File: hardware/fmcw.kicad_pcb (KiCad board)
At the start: 4 copper layers, 123.2 x 49.5 mm, 439 parts, among them CON1 SD_Card_DM3BT, CON2 BARREL_JACK, P1 SMA, P10 CONN_01X01, P11 CONN_01X01, P12 CONN_01X01, P13 CONN_01X01, P14 CONN_01X01, P15 CONN_01X01, P16 CONN_01X01, P2 SMA, P3 CONN_02X04, P4 CONN_02X04, P5 CONN_01X01, P6 CONN_01X01, P7 CONN_01X01, P8 CONN_01X01, P9 CONN_01X01, Q1 RE1C002UN, Q2 DNP(RE1C002UN), SW2 SW_PUSH, U1 ADF4158, U10 HMC431LP4, U11 SKY65404, U12 PAT1220-6dB, U13 TRF37A73, U15 SMA, U16 SKY65404, U17 L7980, U18 L7980, U19 L7980, U2 LP5907-1.8, U20 LP5907-3.0, U21 LP2985A-10DBVR, U22 TPS7A91, U23 TPS7A91, U24 TPS7A91, U25 MIC5301-3.3, U26 5400BL15B050E, U27 5400BL15B050E, U28 5400BL15B050E, U29 ADL5802, U3 PAT1220-6dB, U30 XC7A15T-1FTG256C, U31 USB-MICRO, U32 93LC46B, U33 FT2232H, U34 ADA4940-2, U35 ADA4940-2, U37 SE2567L, U38 TPS7A91, U39 LP5907-3.0, U4 KT2520K, U40 W25Q32JV, U5 NC7S04P5X, U6 NB3N551, U7 TLV172DCK, U8 LTC2292, U9 TRF37A73, Y1 ABM10-167-12.000MHZ-T3

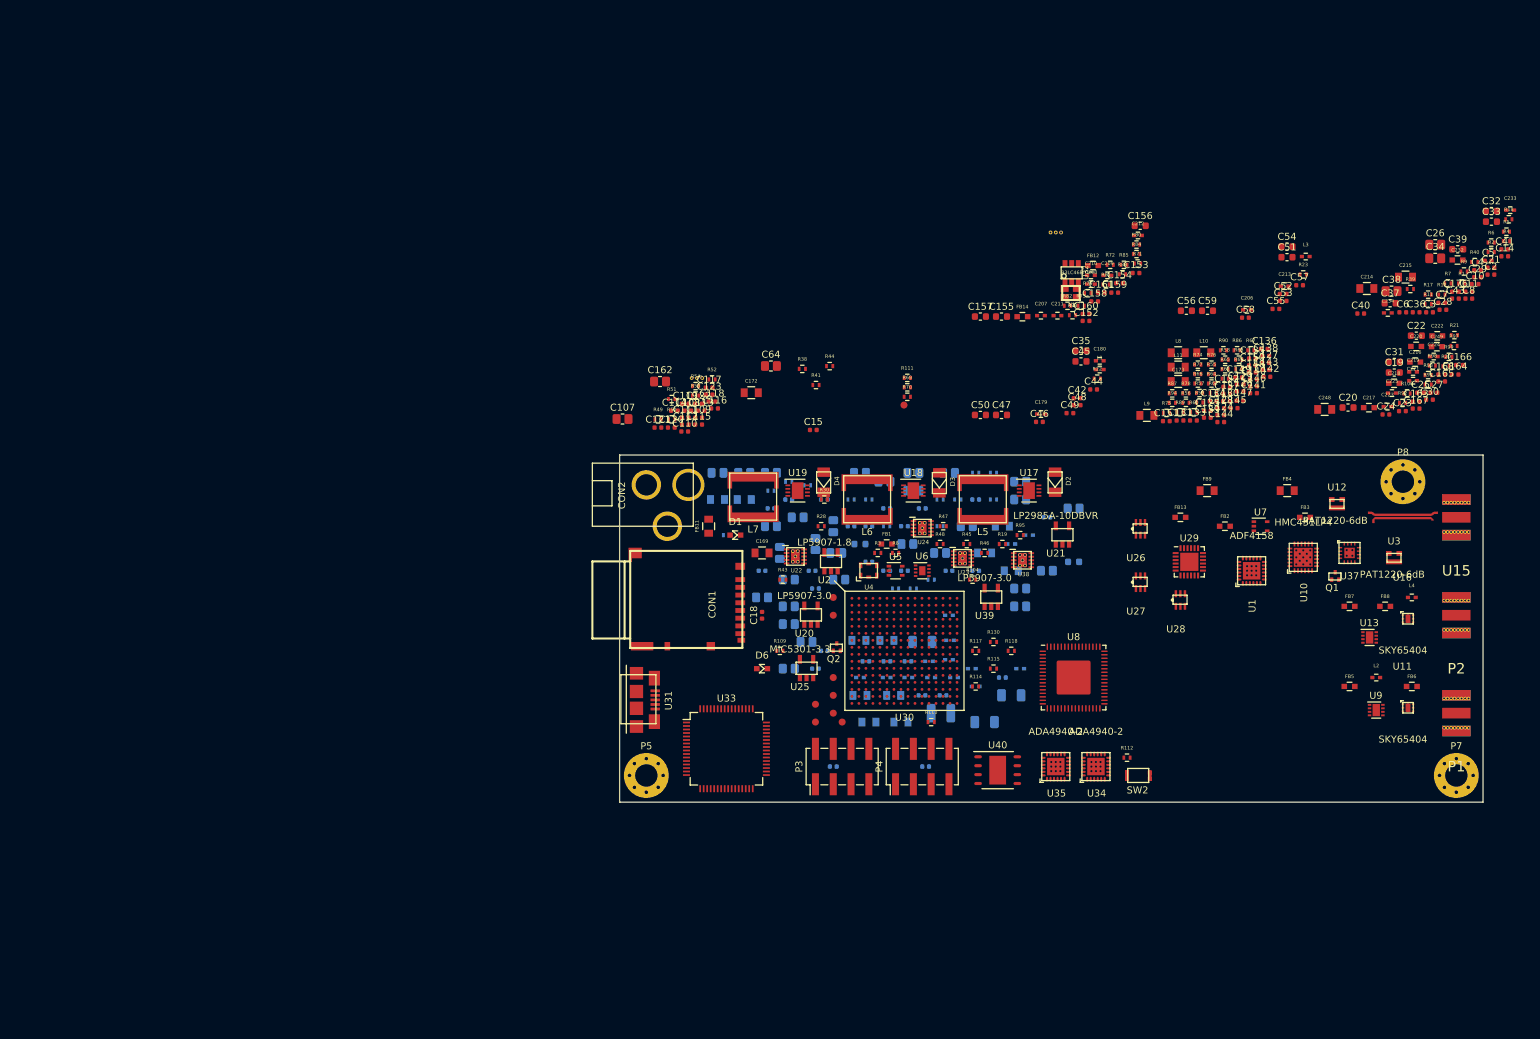
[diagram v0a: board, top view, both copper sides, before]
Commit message: Modularized LaTeX documentation.
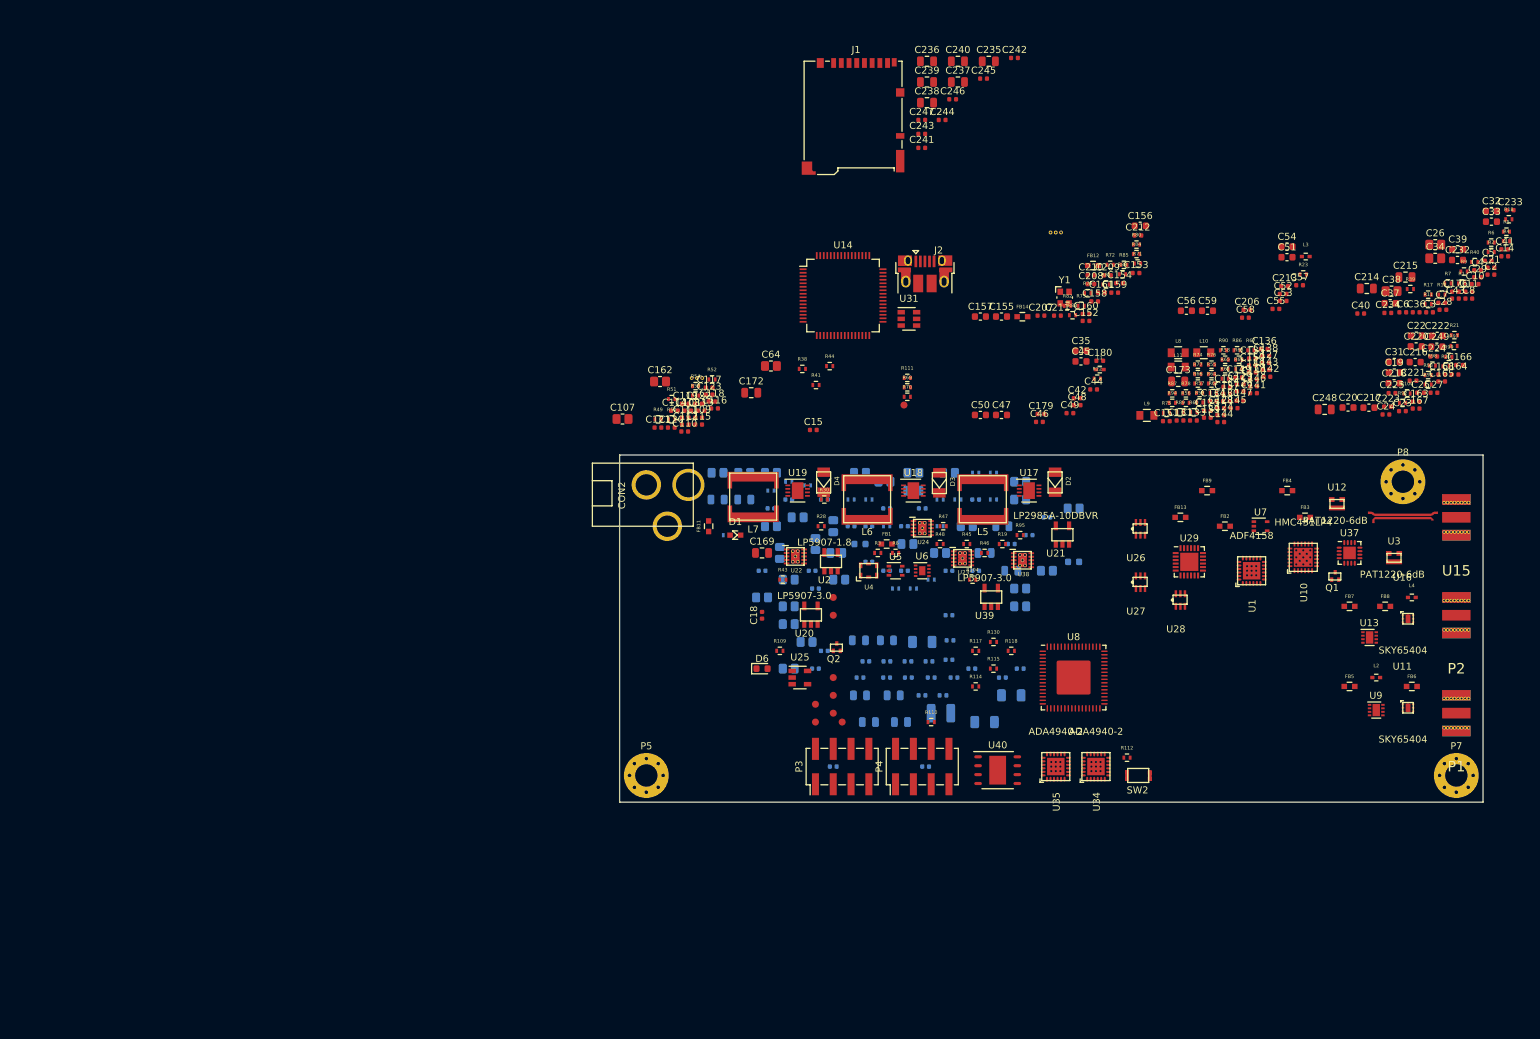
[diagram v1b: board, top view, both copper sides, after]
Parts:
- removed C219: 100n, fmcw3:C_0402b
- removed C250: 470n, fmcw3:C_0402b
- removed C30: 100n, Capacitor_SMD:C_0402_1005Metric
- removed CON1: SD_Card_DM3BT, fmcw3:DM3BT-DSF-PEJS
- removed U30: XC7A15T-1FTG256C, fmcw3:FTG256
- removed U32: 93LC46B, fmcw3:SOT-23-6
- removed U33: FT2232H, Package_QFP:LQFP-64_10x10mm_P0.5mm
- added C235: 4.7u, Capacitor_SMD:C_0805_2012Metric, F.Cu at (163.2, 18.8)
- added C236: 4.7u, Capacitor_SMD:C_0805_2012Metric, F.Cu at (154.3, 18.8)
- added C237: 4.7u, Capacitor_SMD:C_0805_2012Metric, F.Cu at (158.8, 21.7)
- added C238: 4.7u, Capacitor_SMD:C_0805_2012Metric, F.Cu at (154.3, 24.7)
- added C239: 4.7u, Capacitor_SMD:C_0805_2012Metric, F.Cu at (154.3, 21.7)
- added C240: 4.7u, Capacitor_SMD:C_0805_2012Metric, F.Cu at (158.8, 18.8)
- added C241: 470n, Capacitor_SMD:C_0402_1005Metric, F.Cu at (153.6, 31.1)
- added C242: 470n, Capacitor_SMD:C_0402_1005Metric, F.Cu at (166.8, 18.3)
- added C243: 470n, Capacitor_SMD:C_0402_1005Metric, F.Cu at (153.6, 29.1)
- added C244: 470n, Capacitor_SMD:C_0402_1005Metric, F.Cu at (156.5, 27.1)
- added C245: 470n, Capacitor_SMD:C_0402_1005Metric, F.Cu at (162.4, 21.2)
- added C246: 470n, Capacitor_SMD:C_0402_1005Metric, F.Cu at (158.0, 24.2)
- added C247: 470n, Capacitor_SMD:C_0402_1005Metric, F.Cu at (153.6, 27.1)
- added J1: SD_Card, Connector_Card:microSD_HC_Hirose_DM3BT-DSF-PEJS, F.Cu at (143.8, 26.6)
- added J2: USB_B_Micro, Connector_USB:USB_Micro-B_Amphenol_10103594-0001LF_Horizontal, F.Cu at (154.1, 49.1)
- added U14: FT2232H, Package_QFP:LQFP-64_10x10mm_P0.5mm, F.Cu at (142.4, 52.2)
- C109, C110, C111, C112, C113, C114: value 10p -> 3p
- C169, C172, C173, C177, C178, C183, C185, C186, C188, C194, C195, C214, C215, C227, C230, C231, C248: footprint fmcw3:C_0805b -> Capacitor_SMD:C_0805_2012Metric
- C179, C180, C197, C198, C199, C200, C201, C202, C203, C204, C205, C206, C207, C208, C209, C210, C211, C212, C213, C221, C223, C224, C225, C228, C229, C233, C234, C251, C252: footprint fmcw3:C_0402b -> Capacitor_SMD:C_0402_1005Metric
- C216, C217, C218, C220, C222, C232, C249: footprint fmcw3:C_0603b -> Capacitor_SMD:C_0603_1608Metric
- CON2: footprint fmcw3:EJ508A -> fmcw:EJ508A
- D1: footprint fmcw3:LED_0603 -> fmcw:LED_0603
- D2, D3, D4: footprint fmcw3:SOD-123F -> fmcw:SOD-123F
- D6: footprint fmcw3:LED_0603 -> LED_SMD:LED_0603_1608Metric
- F1, F2: footprint fmcw3:RF_via -> fmcw:RF_via
- FB1, FB12, FB13, FB14, FB2, FB3, FB5, FB6, FB7, FB8: footprint fmcw3:C_0603b -> fmcw:C_0603b
- FB11, FB4, FB9: footprint fmcw3:C_0805b -> fmcw:C_0603b
- L1, L2, L3, L4: footprint fmcw3:C_0402b -> fmcw:C_0402b
- L10, L11, L8, L9: footprint fmcw3:C_0805b -> fmcw:C_0805b
- L5, L6, L7: footprint fmcw3:SRR6040A -> fmcw:SRR6040A
- P1, P2, U15: footprint fmcw3:CONSMA003.062 -> fmcw:CONSMA003.062
- P10, P11, P12, P13, P14, P15, P16, P6, P9: footprint fmcw3:TP_1.00 -> fmcw:TP_1.00
- P5, P7, P8: footprint fmcw3:MountingHole_3.2mm_M3_Pad_Via_mod -> fmcw:MountingHole_3.2mm_M3_Pad_Via_mod
- Q1, Q2: footprint fmcw3:SOT-416 -> fmcw:SOT-416
- R1, R100, R101, R103, R104, R109, R11, R110, R111, R112, R114, R115, R117, R118, R12, R13, R130, R15, R16, R17, R18, R19, R2, R20, R21, R22, R23, R24, R25, R26, R27, R28, R29, R3, R30, R31, R32, R33, R34, R35, R36, R37, R38, R39, R4, R40, R41, R42, R43, R44, R45, R46, R47, R48, R49, R5, R50, R51, R52, R53, R54, R55, R56, R57, R58, R59, R6, R60, R61, R62, R63, R64, R65, R66, R67, R68, R69, R7, R70, R71, R72, R73, R74, R75, R76, R77, R78, R79, R8, R80, R81, R82, R83, R84, R85, R86, R87, R88, R89, R9, R90, R91, R92, R93, R94, R95, R97, R98, R99: footprint fmcw3:R_0402b -> fmcw:R_0402b
- SW2: footprint fmcw3:EVP-AWBA2A -> fmcw:EVP-AWBA2A
- U1, U34, U35: footprint fmcw3:VFQFN-24 -> fmcw:VFQFN-24
- U10: footprint fmcw3:VQFN-24 -> fmcw:VQFN-24
- U11, U16: footprint fmcw3:XFDFN-6 -> fmcw:XFDFN-6
- U12, U3: footprint fmcw3:PAT1220 -> fmcw:PAT1220
- U13, U9: footprint fmcw3:DFN-8-1EP_2x2mm_Pitch0.5mm -> fmcw:DFN-8-1EP_2x2mm_Pitch0.5mm
- U2, U20, U21, U39: footprint fmcw3:SOT-23-5 -> fmcw:SOT-23-5
- U22, U23, U24, U38: footprint fmcw3:SON-10_2.5x2.5mm -> fmcw:SON-10_2.5x2.5mm
- U25: footprint fmcw3:SOT-23-5 -> Package_TO_SOT_SMD:SOT-23-5
- U26, U27, U28: footprint fmcw3:5400BL15B050E -> fmcw:5400BL15B050E
- U31: value USB-MICRO -> 93LCxxB; footprint fmcw3:USB_MICRO -> Package_TO_SOT_SMD:SOT-23-6
- U37: footprint fmcw3:MGA-25203 -> Package_DFN_QFN:QFN-16-1EP_3x3mm_P0.5mm_EP1.8x1.8mm
- U4: footprint fmcw3:KT2520K -> fmcw:KT2520K
- U6: footprint fmcw3:DFN-8 -> fmcw:DFN-8
- Y1: footprint fmcw3:ABM10 -> Crystal:Crystal_SMD_Abracon_ABM10-4Pin_2.5x2.0mm
- Z1: footprint fmcw3:coupler -> fmcw:coupler
- moved U31 65.3 mm to (151.8, 55.5), turned to 0 degrees
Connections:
- C205 pad 1: /1V8 -> GND
- C205 pad 2: GND -> /1V8
- FB1 pad 1: /3V3D -> Net-(C15-Pad1)
- FB1 pad 2: Net-(C15-Pad1) -> /3V3D
- FB11 pad 1: Net-(C64-Pad1) -> /power/12V
- FB11 pad 2: /power/12V -> Net-(C64-Pad1)
- FB13 pad 1: /5V -> /mixer/5VF
- FB13 pad 2: /mixer/5VF -> /5V
- FB14 pad 1: /3V3D -> Net-(C157-Pad1)
- FB14 pad 2: Net-(C157-Pad1) -> /3V3D
- FB2 pad 1: /5V -> Net-(C6-Pad1)
- FB2 pad 2: Net-(C6-Pad1) -> /5V
- FB3 pad 1: /3V0 -> Net-(C26-Pad1)
- FB3 pad 2: Net-(C26-Pad1) -> /3V0
- FB4 pad 1: /3V3A -> Net-(C37-Pad2)
- FB4 pad 2: Net-(C37-Pad2) -> /3V3A
- FB5 pad 1: /3V0 -> Net-(C179-Pad1)
- FB5 pad 2: Net-(C179-Pad1) -> /3V0
- FB6 pad 1: /3V0 -> Net-(C49-Pad1)
- FB6 pad 2: Net-(C49-Pad1) -> /3V0
- FB7 pad 1: /3V0 -> Net-(C206-Pad1)
- FB7 pad 2: Net-(C206-Pad1) -> /3V0
- FB8 pad 1: /3V0 -> Net-(C58-Pad1)
- FB8 pad 2: Net-(C58-Pad1) -> /3V0
- FB9 pad 1: Net-(C232-Pad2) -> /4V5
- FB9 pad 2: /4V5 -> Net-(C232-Pad2)
- U31 pad 1: /fpga/usb/USB_5V -> /fpga/usb/EECS
- U31 pad 2: /fpga/usb/USBDM -> /fpga/usb/EECLK
- U31 pad 3: /fpga/usb/USBDP -> /fpga/usb/EEDATA
- U31 pad 4: Net-(U31-Pad4) -> /fpga/usb/DO
- U8 pad 24: Net-(U8-Pad24) -> (no net)
- U8 pad 25: Net-(U8-Pad25) -> (no net)
- U8 pad 26: Net-(U8-Pad26) -> (no net)
- U8 pad 27: Net-(U8-Pad27) -> (no net)
- U8 pad 28: Net-(U8-Pad28) -> (no net)
- U8 pad 29: Net-(U8-Pad29) -> (no net)
- U8 pad 30: Net-(U8-Pad30) -> (no net)
- U8 pad 33: Net-(U8-Pad33) -> (no net)
- U8 pad 34: Net-(U8-Pad34) -> (no net)
- U8 pad 35: Net-(U8-Pad35) -> (no net)
- U8 pad 36: Net-(U8-Pad36) -> (no net)
- U8 pad 37: Net-(U8-Pad37) -> (no net)
- U8 pad 38: Net-(U8-Pad38) -> (no net)
- U8 pad 39: Net-(U8-Pad39) -> (no net)
- U8 pad 41: Net-(U8-Pad41) -> (no net)
- U8 pad 42: Net-(U8-Pad42) -> (no net)
- Y1 pad 2: Net-(Y1-Pad2) -> Net-(C209-Pad1)
- Y1 pad 3: Net-(C209-Pad1) -> (no net)
- Y1 pad 4: Net-(Y1-Pad4) -> (no net)
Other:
- net class Default: clearance 0.13 -> 0.127; trace_width 0.15 -> 0.1524; via_dia 0.46 -> 0.4572
- rule pad_to_mask_clearance: 0.2 -> 0.0508
- rule trace_clearance: 0.13 -> 0.127
- rule trace_min: 0.15 -> 0.1524
- rule via_min_size: 0.46 -> 0.4572

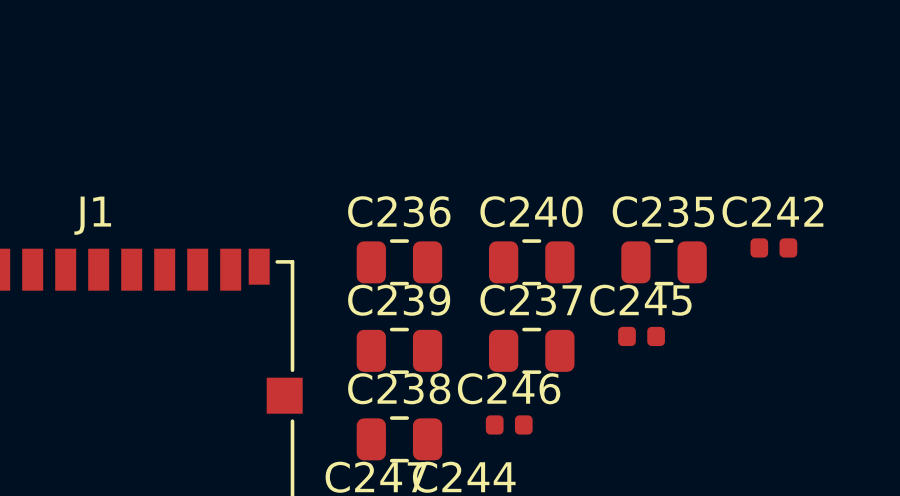
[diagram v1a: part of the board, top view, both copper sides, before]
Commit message: Documentation for TPS5420D buck converter.
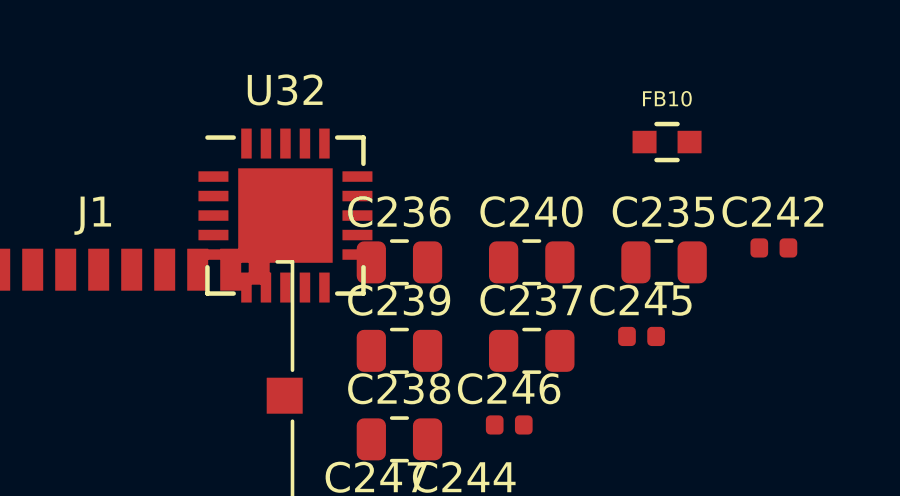
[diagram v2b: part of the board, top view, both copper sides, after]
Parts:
- added FB10: CIC21P101NE, fmcw:C_0603b, F.Cu at (163.3, 14.7)
- added U32: TPS7A7200RGW, Package_DFN_QFN:Texas_VQFN-RGW-20, F.Cu at (150.5, 17.2)
- C33: value DNP -> 10p
- C34, C86: value 10u -> DNP
- C36: value 10p -> 10u
- C41: value 100p -> 2.2u
- C60, C61: value 10u -> 100p
- C63, C96: value 10n -> DNP
- C65: value 10n -> 10u
- C66: value 10n -> 2.2u
- C67: value 39p -> 100p
- C69: value 68p -> 10u
- C73: value 15n -> 10u
- C74: value 8.2n -> 10u
- C75: value 4.7n -> 10u
- C77, C78, C82, C84: value 10u -> 10n
- C79, C80: value 10u -> 6TPH100MAEA
- C81: value DNP -> 10u
- C83: value 10u -> 100n
- C90: value 100n -> 10u
- D2, D3: value SS13FL -> SS24FL
- L5, L7: value 33u (SRR6040A-330M) -> SRR1210A-330M
- R18: value 4.7k -> 1.5k
- R19: value 6.8k -> 5.11k
- R25: value 68k -> 10k
- R26: value 68k -> 2.8k
- R27: value 15k -> 100k
- R28: value 59k -> 2.55k
- R29: value 6.8k -> 10.2k
- R30: value 8.2k -> 280k
- R31: value DNP -> 30.9k
- U17: value L7980 -> SE5004L
- U18, U19: value L7980 -> TPS5420D
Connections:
- C33 pad 1: GND -> Net-(C33-Pad1)
- C33 pad 2: Net-(C232-Pad2) -> Net-(C30-Pad2)
- C34 pad 2: Net-(C232-Pad2) -> Net-(C34-Pad2)
- C36 pad 1: /tx/EN -> GND
- C36 pad 2: GND -> Net-(C34-Pad2)
- C37 pad 1: GND -> Net-(C37-Pad1)
- C37 pad 2: Net-(C37-Pad2) -> GND
- C38 pad 1: GND -> Net-(C37-Pad1)
- C38 pad 2: Net-(C37-Pad2) -> GND
- C39 pad 1: GND -> Net-(C37-Pad1)
- C39 pad 2: Net-(C37-Pad2) -> GND
- C40 pad 1: GND -> Net-(C37-Pad1)
- C40 pad 2: Net-(C37-Pad2) -> GND
- C41 pad 2: Net-(C37-Pad2) -> Net-(C34-Pad2)
- C60 pad 1: /power/12V -> GND
- C60 pad 2: GND -> Net-(C34-Pad2)
- C61 pad 1: /power/12V -> GND
- C61 pad 2: GND -> Net-(C34-Pad2)
- C63 pad 1: Net-(C63-Pad1) -> GND
- C65 pad 1: Net-(C65-Pad1) -> GND
- C65 pad 2: Net-(C65-Pad2) -> Net-(C63-Pad2)
- C66 pad 1: Net-(C66-Pad1) -> GND
- C66 pad 2: Net-(C66-Pad2) -> Net-(C63-Pad2)
- C67 pad 1: Net-(C67-Pad1) -> GND
- C68 pad 1: Net-(C68-Pad1) -> GND
- C68 pad 2: Net-(C65-Pad2) -> Net-(C63-Pad2)
- C69 pad 1: Net-(C69-Pad1) -> /power/12V
- C69 pad 2: Net-(C66-Pad2) -> GND
- C73 pad 1: Net-(C73-Pad1) -> /power/12V
- C73 pad 2: Net-(C63-Pad2) -> GND
- C74 pad 1: Net-(C74-Pad1) -> /power/12V
- C74 pad 2: Net-(C65-Pad2) -> GND
- C75 pad 1: Net-(C75-Pad1) -> /power/12V
- C75 pad 2: Net-(C66-Pad2) -> GND
- C76 pad 1: /1V0 -> /power/12V
- C77 pad 1: /3V6 -> Net-(C77-Pad1)
- C77 pad 2: GND -> Net-(C77-Pad2)
- C78 pad 1: /1V0 -> Net-(C78-Pad1)
- C78 pad 2: GND -> Net-(C78-Pad2)
- C79 pad 1: /power/5V6 -> /power/3V6
- C80 pad 1: /3V6 -> /power/5V6
- C81 pad 1: /3V6 -> /power/3V6
- C83 pad 1: /power/5V6 -> Net-(C83-Pad1)
- C84 pad 1: /power/5V6 -> /1V0
- C84 pad 2: GND -> Net-(C84-Pad2)
- C85 pad 1: /3V6 -> /power/3V6
- C86 pad 1: /power/5V6 -> /5V
- C86 pad 2: GND -> Net-(C86-Pad2)
- C87 pad 1: /3V6 -> /power/3V6
- C88 pad 1: /3V6 -> /power/3V6
- C90 pad 1: Net-(C90-Pad1) -> /1V0
- C94 pad 1: /3V6 -> /power/3V6
- C96 pad 1: /5V -> /1V0
- C96 pad 2: Net-(C96-Pad2) -> GND
- D2 pad 1: Net-(D2-Pad1) -> Net-(C77-Pad1)
- D3 pad 1: Net-(D3-Pad1) -> Net-(C78-Pad1)
- FB4 pad 1: Net-(C37-Pad2) -> Net-(C37-Pad1)
- FB4 pad 2: /3V3A -> /5V
- FB9 pad 1: /4V5 -> Net-(C34-Pad2)
- FB9 pad 2: Net-(C232-Pad2) -> /5V
- J2 pad 6: Net-(J2-Pad6) -> GND
- L5 pad 1: Net-(D2-Pad1) -> Net-(C77-Pad1)
- L5 pad 2: /1V0 -> /power/3V6
- L7 pad 1: Net-(D4-Pad1) -> Net-(C78-Pad1)
- Q1 pad 3: /tx/EN -> Net-(C30-Pad2)
- R104 pad 1: /3V6 -> /power/3V6
- R18 pad 2: /tx/EN -> Net-(C30-Pad2)
- R19 pad 1: /4V5 -> Net-(R14-Pad2)
- R19 pad 2: Net-(C229-Pad2) -> GND
- R24 pad 1: /3V6 -> /power/3V6
- R25 pad 1: Net-(R25-Pad1) -> /power/5V6
- R25 pad 2: GND -> Net-(R25-Pad2)
- R26 pad 1: Net-(R26-Pad1) -> Net-(R25-Pad2)
- R27 pad 1: Net-(C67-Pad1) -> Net-(R27-Pad1)
- R27 pad 2: Net-(C63-Pad1) -> /5V
- R28 pad 1: Net-(R28-Pad1) -> /1V0
- R28 pad 2: GND -> Net-(C84-Pad2)
- R29 pad 1: Net-(C68-Pad1) -> Net-(C84-Pad2)
- R29 pad 2: Net-(C65-Pad1) -> GND
- R30 pad 1: Net-(C69-Pad1) -> /5V
- R30 pad 2: Net-(C66-Pad1) -> Net-(C86-Pad2)
- R31 pad 1: /power/SYNC -> Net-(C86-Pad2)
- R31 pad 2: Net-(R31-Pad2) -> GND
- U17 pad 1: Net-(D2-Pad1) -> Net-(U17-Pad1)
- U17 pad 2: Net-(R31-Pad2) -> GND
- U17 pad 3: Net-(R101-Pad1) -> Net-(U12-Pad1)
- U17 pad 4: Net-(C67-Pad1) -> GND
- U17 pad 5: Net-(C63-Pad2) -> Net-(C30-Pad2)
- U17 pad 6: Net-(R25-Pad1) -> Net-(C33-Pad1)
- U17 pad 7: GND -> Net-(C30-Pad1)
- U17 pad 8: /power/12V -> Net-(C34-Pad2)
- U17 pad 9: GND -> Net-(C63-Pad2)
- U18 pad 1: Net-(D3-Pad1) -> Net-(C77-Pad2)
- U18 pad 2: /power/SYNC -> Net-(U18-Pad2)
- U18 pad 3: /power/12V -> Net-(U18-Pad3)
- U18 pad 4: Net-(C68-Pad1) -> Net-(R14-Pad2)
- U18 pad 5: Net-(C65-Pad2) -> Net-(U18-Pad5)
- U18 pad 6: Net-(R26-Pad1) -> GND
- U18 pad 7: GND -> /power/12V
- U18 pad 8: /power/12V -> Net-(C77-Pad1)
- U18 pad 9: GND -> (no net)
- U19 pad 1: Net-(D4-Pad1) -> Net-(C78-Pad2)
- U19 pad 2: /power/SYNC -> Net-(U19-Pad2)
- U19 pad 3: /power/12V -> Net-(U19-Pad3)
- U19 pad 4: Net-(C69-Pad1) -> Net-(R25-Pad2)
- U19 pad 5: Net-(C66-Pad2) -> Net-(U19-Pad5)
- U19 pad 6: Net-(R28-Pad1) -> GND
- U19 pad 7: GND -> /power/12V
- U19 pad 8: /power/12V -> Net-(C78-Pad1)
- U19 pad 9: GND -> (no net)
- U20 pad 1: /3V6 -> /power/3V6
- U20 pad 3: /3V6 -> /power/3V6
- U22 pad 1: /5V -> /1V0
- U22 pad 10: /power/5V6 -> /power/3V6
- U22 pad 2: /5V -> /1V0
- U22 pad 3: Net-(C96-Pad2) -> Net-(C84-Pad2)
- U22 pad 6: /power/5V6 -> /power/3V6
- U22 pad 7: /power/5V6 -> /power/3V6
- U22 pad 8: Net-(C90-Pad1) -> Net-(C83-Pad1)
- U22 pad 9: /power/5V6 -> /power/3V6
- U23 pad 10: /3V6 -> /power/3V6
- U23 pad 6: /3V6 -> /power/3V6
- U23 pad 9: /3V6 -> /power/3V6
- U24 pad 10: /3V6 -> /power/3V6
- U24 pad 6: /3V6 -> /power/3V6
- U24 pad 7: /3V6 -> /power/3V6
- U24 pad 9: /3V6 -> /power/3V6
- U25 pad 1: /3V6 -> /power/3V6
- U8 pad 24: (no net) -> Net-(U8-Pad24)
- U8 pad 25: (no net) -> Net-(U8-Pad25)
- U8 pad 26: (no net) -> Net-(U8-Pad26)
- U8 pad 27: (no net) -> Net-(U8-Pad27)
- U8 pad 28: (no net) -> Net-(U8-Pad28)
- U8 pad 29: (no net) -> Net-(U8-Pad29)
- U8 pad 30: (no net) -> Net-(U8-Pad30)
- U8 pad 33: (no net) -> Net-(U8-Pad33)
- U8 pad 34: (no net) -> Net-(U8-Pad34)
- U8 pad 35: (no net) -> Net-(U8-Pad35)
- U8 pad 36: (no net) -> Net-(U8-Pad36)
- U8 pad 37: (no net) -> Net-(U8-Pad37)
- U8 pad 38: (no net) -> Net-(U8-Pad38)
- U8 pad 39: (no net) -> Net-(U8-Pad39)
- U8 pad 41: (no net) -> Net-(U8-Pad41)
- U8 pad 42: (no net) -> Net-(U8-Pad42)
- Z1 pad 1: Net-(U37-Pad11) -> Net-(U17-Pad13)
